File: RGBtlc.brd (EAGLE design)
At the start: 33 x 53.3 mm, 18 parts, among them U1 TLC5940-NT

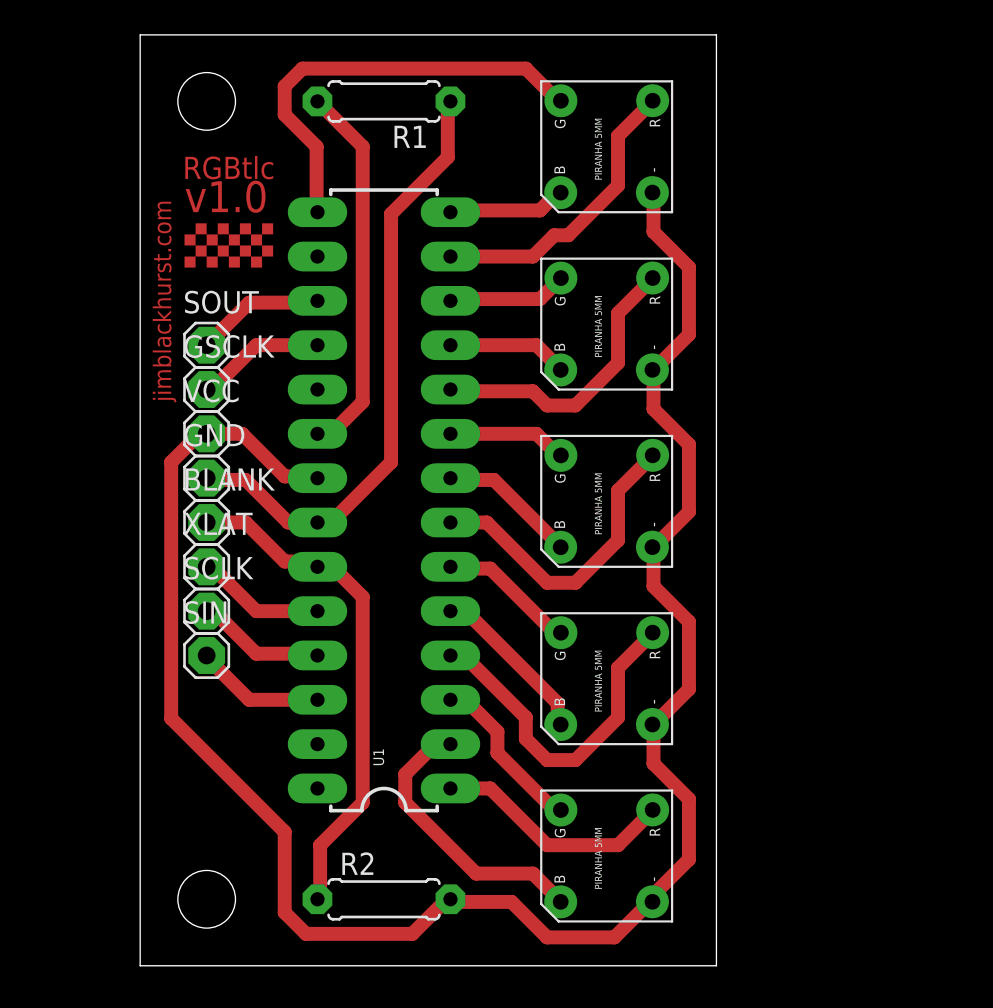
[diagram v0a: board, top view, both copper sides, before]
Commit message: V2, now with daisy chain ports
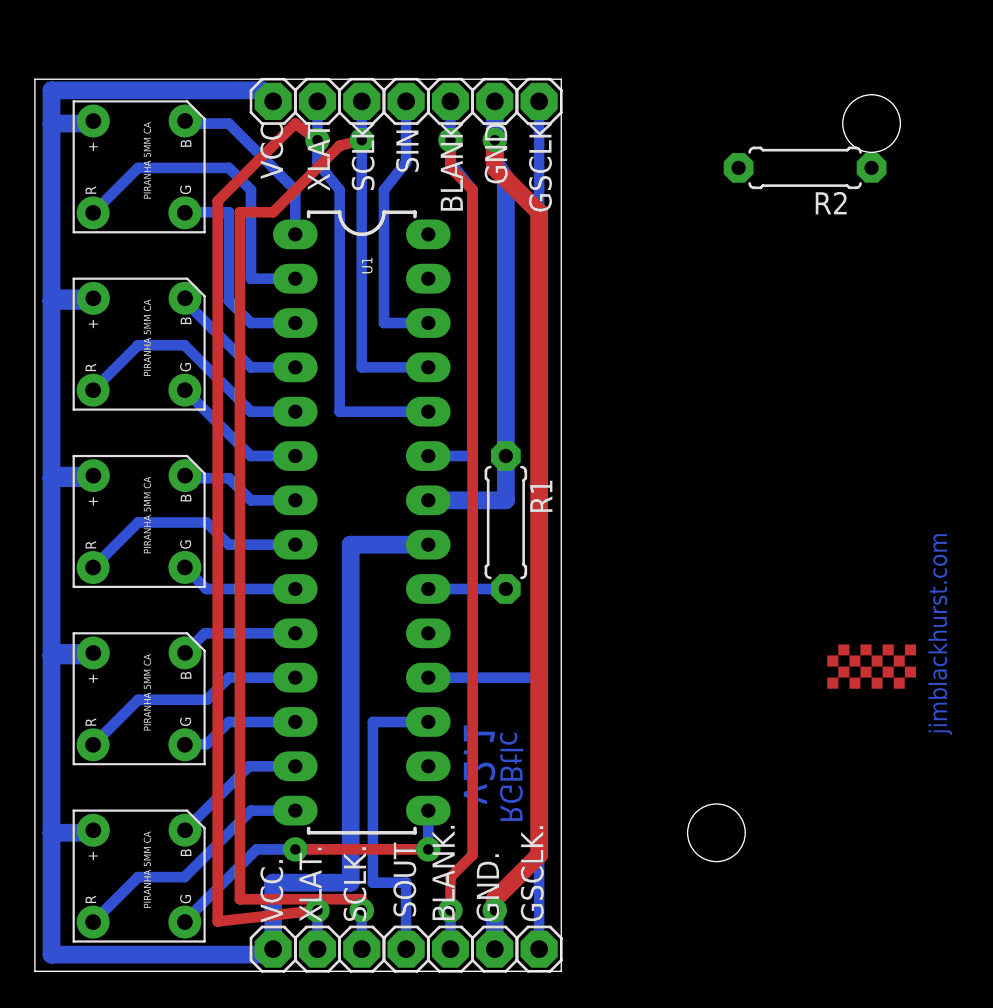
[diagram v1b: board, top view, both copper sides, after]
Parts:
- added BLANK., GND., GSCLK., SCLK., VCC., XLAT.: (no value), pinhead:1X01
- U$1, U$2, U$3, U$4, U$5: value LED_PIRANHA_5MM -> (none); device SparkFun-LED:LED_PIRANHA_5MM -> jim:LED_PIRANHA_5MM
- moved JP4 58.5 mm to (73.7, 53.3), turned to 180 degrees
- moved JP1 51.1 mm to (64.8, 12.7), turned to 180 degrees
- moved U$5 49.7 mm to (31.8, 10.2), turned to 270 degrees
- moved R2 48.4 mm to (69.8, 50.8), turned to 180 degrees
- moved U$1 47.6 mm to (31.8, 50.8), turned to 270 degrees
- moved SOUT 36.4 mm to (47.0, 6.03), turned to 180 degrees
- moved U$4 34.3 mm to (31.8, 20.3), turned to 270 degrees
- moved SIN 33.7 mm to (47.0, 54.6), turned to 180 degrees
- moved U$2 32.8 mm to (31.8, 40.6), turned to 270 degrees
- moved SCLK 30.5 mm to (44.5, 54.6), turned to 180 degrees
- moved BLANK 27.9 mm to (49.5, 54.6), turned to 180 degrees
- moved XLAT 27.4 mm to (41.9, 54.6), turned to 180 degrees
- moved GND 27.2 mm to (52.1, 54.6), turned to 180 degrees
- moved U$3 26.7 mm to (31.8, 30.5), turned to 270 degrees
- moved GSCLK 25.2 mm to (54.6, 54.6), turned to 180 degrees
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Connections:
- removed net N$10: U$3.R, U1.7
- new net N$23: U$3.R, U1.8
- net GND: now also GND..1
- net N$12: now also U$2.R; no longer U$2.B
- net N$13: now also U$2.B; no longer U$2.R
- net N$15: now also U$1.R; no longer U$1.B
- net N$16: now also U$1.B; no longer U$1.R
- net N$17: now also SCLK..1
- net N$19: now also XLAT..1
- net N$2: now also U$5.R; no longer U$5.B
- net N$20: now also GSCLK..1
- net N$3: now also U$5.B; no longer U$5.R
- net N$4: now also U1.7; no longer U1.8
- net N$6: now also U$4.R; no longer U$4.B
- net N$7: now also U$4.B; no longer U$4.R
- net N$9: now also BLANK..1; no longer R2.1
- net VCC: now also U$1.+, U$2.+, U$3.+, U$4.+, U$5.+, VCC..1; no longer R2.2, U$1.-, U$2.-, U$3.-, U$4.-, U$5.-
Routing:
- net N$19: track 7.46 -> 80.4 mm, vias 0 -> 2
- net N$17: track 7.42 -> 76.9 mm, vias 0 -> 2
- net N$20: track 7.46 -> 54.9 mm
- net N$9: track 29.2 -> 70.7 mm, vias 0 -> 2
- net GND: track 35.2 -> 76.0 mm, vias 0 -> 2
- net N$10: track 17.7 -> 0.00 mm
- net N$22: track 21.6 -> 4.45 mm
- net VCC: track 110.5 -> 127.0 mm
- net N$23: track 0.00 -> 13.2 mm
- net N$13: track 19.5 -> 8.09 mm
- net N$21: track 7.42 -> 18.1 mm
- net N$7: track 16.7 -> 6.78 mm
- net N$3: track 17.0 -> 7.83 mm
- net N$18: track 7.46 -> 15.7 mm
- net N$2: track 6.80 -> 14.2 mm
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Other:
- board size 33 x 53.3 mm -> 30.2 x 51.1 mm
- board text added: "v2.1"
- board text removed: "v1.0"
